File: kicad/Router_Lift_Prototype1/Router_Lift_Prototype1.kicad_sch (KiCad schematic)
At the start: 31 parts, among them J1 Conn_01x02, J10 Conn_01x02, J11 Conn_01x04, J2 Conn_01x02, J3 Conn_01x06, J4 Conn_01x06, J5 Conn_01x06, J6 Conn_01x02, J7 Conn_01x02, J8 Conn_01x02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

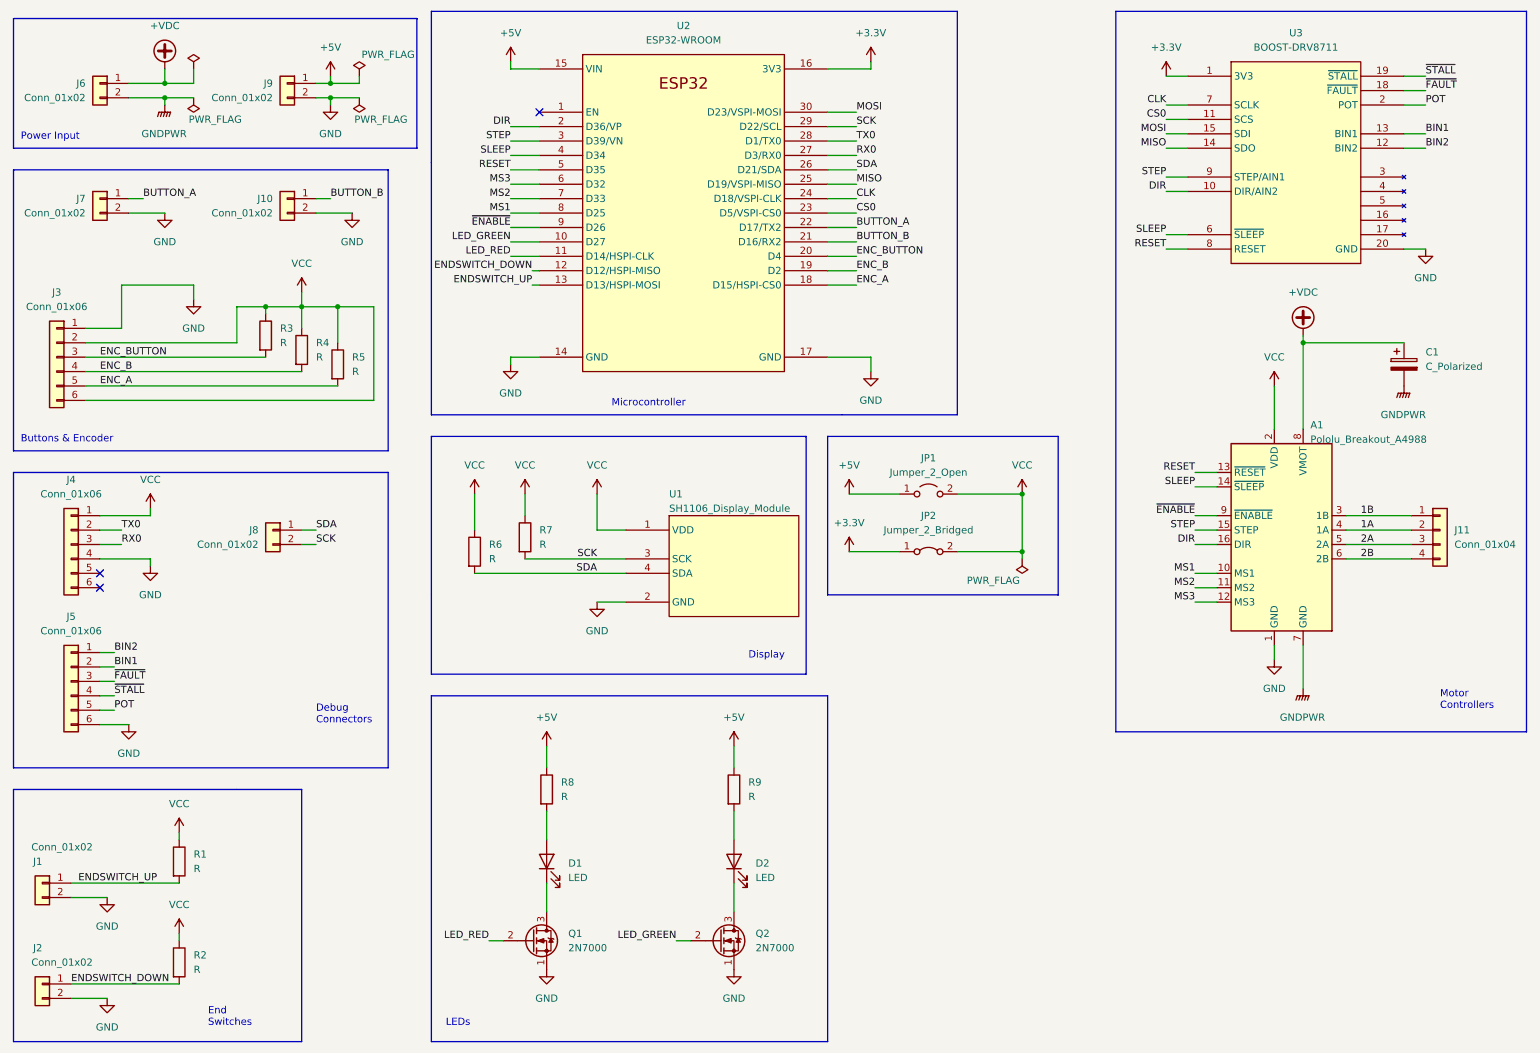
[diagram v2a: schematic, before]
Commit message: Finished routing before curving tracks and review
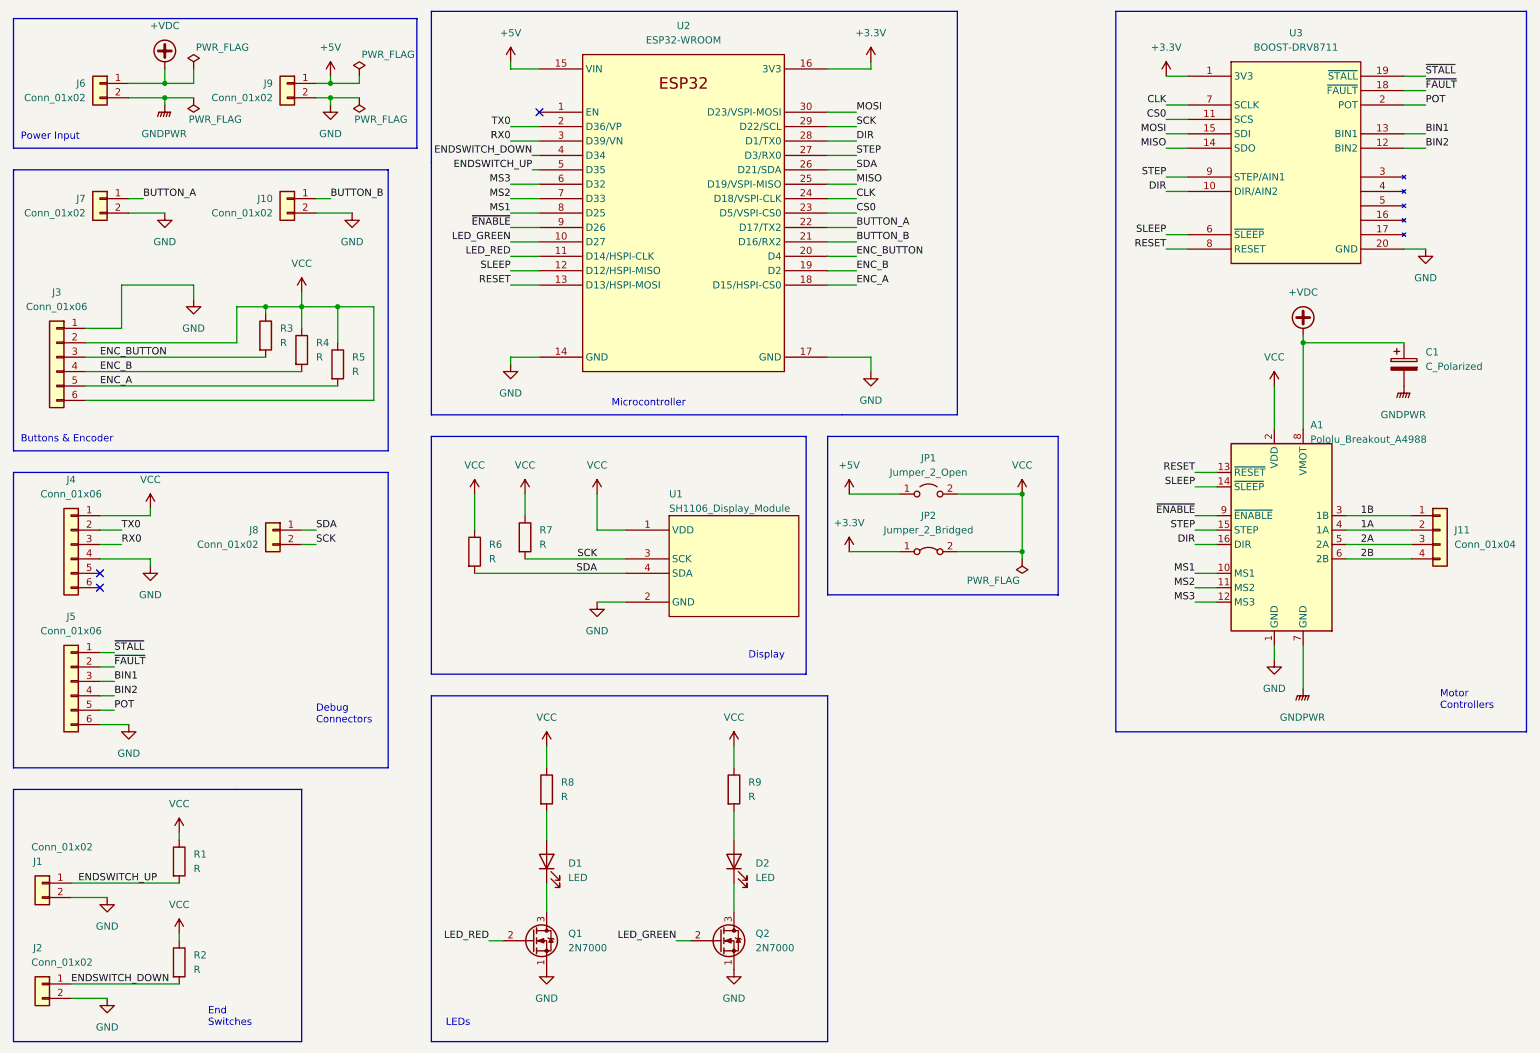
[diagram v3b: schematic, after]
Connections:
- net +5V: no longer R8.1, R9.1
- net BIN1: now also J5.3 (Pin_3); no longer J5.2 (Pin_2)
- net BIN2: now also J5.4 (Pin_4); no longer J5.1 (Pin_1)
- net DIR: now also U2.28 (D1/TX0); no longer U2.2 (D36/VP)
- net ENDSWITCH_DOWN: now also U2.4 (D34); no longer U2.12 (D12/HSPI-MISO)
- net ENDSWITCH_UP: now also U2.5 (D35); no longer U2.13 (D13/HSPI-MOSI)
- net RESET: now also U2.13 (D13/HSPI-MOSI); no longer U2.5 (D35)
- net RX0: now also U2.3 (D39/VN); no longer U2.27 (D3/RX0)
- net SLEEP: now also U2.12 (D12/HSPI-MISO); no longer U2.4 (D34)
- net STEP: now also U2.27 (D3/RX0); no longer U2.3 (D39/VN)
- net TX0: now also U2.2 (D36/VP); no longer U2.28 (D1/TX0)
- net VCC: now also R8.1, R9.1
- net ~{FAULT}: now also J5.2 (Pin_2); no longer J5.3 (Pin_3)
- net ~{STALL}: now also J5.1 (Pin_1); no longer J5.4 (Pin_4)
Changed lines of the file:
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@@
     (stroke (width 0) (type default) (color 0 0 0 0))
   )
-  (wire (pts (xy 107.95 62.23) (xy 109.22 62.23))
+  (wire (pts (xy 104.14 62.23) (xy 109.22 62.23))
     (stroke (width 0) (type default) (color 0 0 0 0))
   )
@@
     (stroke (width 0) (type default) (color 0 0 0 0))
   )
-  (wire (pts (xy 107.95 59.69) (xy 109.22 59.69))
+  (wire (pts (xy 104.14 59.69) (xy 109.22 59.69))
     (stroke (width 0) (type default) (color 0 0 0 0))
   )
@@
     (stroke (width 0) (type default) (color 0 0 0 0))
   )
-  (wire (pts (xy 104.14 41.91) (xy 109.22 41.91))
+  (wire (pts (xy 107.95 41.91) (xy 109.22 41.91))
     (stroke (width 0) (type default) (color 0 0 0 0))
   )
@@
     (stroke (width 0) (type default) (color 0 0 0 0))
   )
-  (wire (pts (xy 104.14 39.37) (xy 109.22 39.37))
+  (wire (pts (xy 107.95 39.37) (xy 109.22 39.37))
     (stroke (width 0) (type default) (color 0 0 0 0))
   )
@@
     (effects (font (size 1.27 1.27)) (justify left bottom))
   )
-  (label "ENDSWITCH_DOWN" (at 107.95 59.69 180)
+  (label "SLEEP" (at 104.14 59.69 180)
     (effects (font (size 1.27 1.27)) (justify right bottom))
   )
@@
     (effects (font (size 1.27 1.27)) (justify right bottom))
   )
-  (label "~{FAULT}" (at 34.29 132.08 0)
+  (label "BIN1" (at 34.29 132.08 0)
     (effects (font (size 1.27 1.27)) (justify left bottom))
   )
@@
     (effects (font (size 1.27 1.27)) (justify right bottom))
   )
-  (label "BIN1" (at 34.29 129.54 0)
+  (label "~{FAULT}" (at 34.29 129.54 0)
     (effects (font (size 1.27 1.27)) (justify left bottom))
   )
@@
     (effects (font (size 1.27 1.27)) (justify right bottom))
   )
-  (label "DIR" (at 104.14 34.29 180)
+  (label "TX0" (at 104.14 34.29 180)
     (effects (font (size 1.27 1.27)) (justify right bottom))
   )
@@
     (effects (font (size 1.27 1.27)) (justify left bottom))
   )
-  (label "RESET" (at 104.14 41.91 180)
-    (effects (font (size 1.27 1.27)) (justify right bottom))
-  )
-  (label "RX0" (at 165.1 39.37 0)
+  (label "ENDSWITCH_UP" (at 107.95 41.91 180)
+    (effects (font (size 1.27 1.27)) (justify right bottom))
+  )
+  (label "STEP" (at 165.1 39.37 0)
     (effects (font (size 1.27 1.27)) (justify left bottom))
   )
@@
     (effects (font (size 1.27 1.27)) (justify left bottom))
   )
-  (label "~{STALL}" (at 34.29 134.62 0)
+  (label "BIN2" (at 34.29 134.62 0)
     (effects (font (size 1.27 1.27)) (justify left bottom))
   )
@@
     (effects (font (size 1.27 1.27)) (justify left bottom))
   )
-  (label "STEP" (at 104.14 36.83 180)
+  (label "RX0" (at 104.14 36.83 180)
     (effects (font (size 1.27 1.27)) (justify right bottom))
   )
@@
     (effects (font (size 1.27 1.27)) (justify left bottom))
   )
-  (label "ENDSWITCH_UP" (at 107.95 62.23 180)
+  (label "RESET" (at 104.14 62.23 180)
     (effects (font (size 1.27 1.27)) (justify right bottom))
   )
@@
     (effects (font (size 1.27 1.27)) (justify left bottom))
   )
-  (label "SLEEP" (at 104.14 39.37 180)
+  (label "ENDSWITCH_DOWN" (at 107.95 39.37 180)
     (effects (font (size 1.27 1.27)) (justify right bottom))
   )
@@
     (effects (font (size 1.27 1.27)) (justify right bottom))
   )
-  (label "BIN2" (at 34.29 127 0)
+  (label "~{STALL}" (at 34.29 127 0)
     (effects (font (size 1.27 1.27)) (justify left bottom))
   )
@@
     (effects (font (size 1.27 1.27)) (justify left bottom))
   )
-  (label "TX0" (at 165.1 36.83 0)
+  (label "DIR" (at 165.1 36.83 0)
     (effects (font (size 1.27 1.27)) (justify left bottom))
   )
@@
   (label "CLK" (at 219.71 30.48 180)
     (effects (font (size 1.27 1.27)) (justify right bottom))
-  )
-  (symbol (lib_id "power:+5V") (at 110.49 143.51 0) (unit 1)
-    (in_bom yes) (on_board yes) (fields_autoplaced)
-    (property "Reference" "#PWR020" (id 0) (at 110.49 147.32 0)
-      (effects (font (size 1.27 1.27)) hide)
-    )
-    (property "Value" "+5V" (id 1) (at 110.49 138.43 0))
-    (property "Footprint" "" (id 2) (at 110.49 143.51 0)
-      (effects (font (size 1.27 1.27)) hide)
-    )
-    (property "Datasheet" "" (id 3) (at 110.49 143.51 0)
-      (effects (font (size 1.27 1.27)) hide)
-    )
-    (pin "1")
   )
   (symbol (lib_id "Connector_Generic:Conn_01x06") (at 24.13 74.93 0) (mirror y) (unit 1)
@@
       (effects (font (size 1.27 1.27)) hide)
     )
-    (property "Value" "" (id 1) (at 53.34 20.32 0))
+    (property "Value" "PWR_FLAG" (id 1) (at 53.34 20.32 0))
     (property "Footprint" "" (id 2) (at 48.26 24.13 0)
       (effects (font (size 1.27 1.27)) hide)
@@
     (pin "1")
   )
-  (symbol (lib_id "power:+5V") (at 143.51 143.51 0) (unit 1)
-    (in_bom yes) (on_board yes) (fields_autoplaced)
-    (property "Reference" "#PWR024" (id 0) (at 143.51 147.32 0)
-      (effects (font (size 1.27 1.27)) hide)
-    )
-    (property "Value" "+5V" (id 1) (at 143.51 138.43 0))
-    (property "Footprint" "" (id 2) (at 143.51 143.51 0)
-      (effects (font (size 1.27 1.27)) hide)
-    )
-    (property "Datasheet" "" (id 3) (at 143.51 143.51 0)
-      (effects (font (size 1.27 1.27)) hide)
-    )
-    (pin "1")
-  )
   (symbol (lib_id "Driver_Motor:BOOST-DRV8711") (at 238.76 22.86 0) (unit 1)
     (in_bom yes) (on_board yes) (fields_autoplaced)
@@
     (pin "2")
   )
+  (symbol (lib_id "power:VCC") (at 143.51 143.51 0) (unit 1)
+    (in_bom yes) (on_board yes) (fields_autoplaced)
+    (property "Reference" "#PWR0101" (id 0) (at 143.51 147.32 0)
+      (effects (font (size 1.27 1.27)) hide)
+    )
+    (property "Value" "VCC" (id 1) (at 143.51 138.43 0))
+    (property "Footprint" "" (id 2) (at 143.51 143.51 0)
+      (effects (font (size 1.27 1.27)) hide)
+    )
+    (property "Datasheet" "" (id 3) (at 143.51 143.51 0)
+      (effects (font (size 1.27 1.27)) hide)
+    )
+    (pin "1")
+  )
   (symbol (lib_id "Connector_Generic:Conn_01x02") (at 21.59 185.42 0) (mirror y) (unit 1)
     (in_bom yes) (on_board yes)
@@
     (pin "1")
   )
+  (symbol (lib_id "power:VCC") (at 110.49 143.51 0) (unit 1)
+    (in_bom yes) (on_board yes) (fields_autoplaced)
+    (property "Reference" "#PWR0102" (id 0) (at 110.49 147.32 0)
+      (effects (font (size 1.27 1.27)) hide)
+    )
+    (property "Value" "VCC" (id 1) (at 110.49 138.43 0))
+    (property "Footprint" "" (id 2) (at 110.49 143.51 0)
+      (effects (font (size 1.27 1.27)) hide)
+    )
+    (property "Datasheet" "" (id 3) (at 110.49 143.51 0)
+      (effects (font (size 1.27 1.27)) hide)
+    )
+    (pin "1")
+  )
   (symbol (lib_id "power:GND") (at 143.51 182.88 0) (unit 1)
     (in_bom yes) (on_board yes) (fields_autoplaced)
@@
       (reference "#PWR019") (unit 1) (value "VCC") (footprint "")
     )
-    (path "/00a71c34-68cb-4c27-a70b-1a03b929fc16"
-      (reference "#PWR020") (unit 1) (value "+5V") (footprint "")
-    )
     (path "/6bb4d235-2725-4be1-ab0a-0431df37ccdd"
       (reference "#PWR021") (unit 1) (value "GND") (footprint "")
@@
       (reference "#PWR023") (unit 1) (value "GND") (footprint "")
     )
-    (path "/4467ef4a-ba48-4fbd-bcde-515863e72e5a"
-      (reference "#PWR024") (unit 1) (value "+5V") (footprint "")
-    )
     (path "/e5e1e167-deb5-49f8-86ac-624780fb22d3"
       (reference "#PWR025") (unit 1) (value "GND") (footprint "")
@@
       (reference "#PWR037") (unit 1) (value "GND") (footprint "")
     )
+    (path "/908f8058-f18e-4794-8f26-b9e7a0a95f81"
+      (reference "#PWR0101") (unit 1) (value "VCC") (footprint "")
+    )
+    (path "/e42a6a7a-8964-45f9-9ec9-6998e392508a"
+      (reference "#PWR0102") (unit 1) (value "VCC") (footprint "")
+    )
     (path "/b9b39cc1-4792-4af5-ad6c-76001dfd95bd"

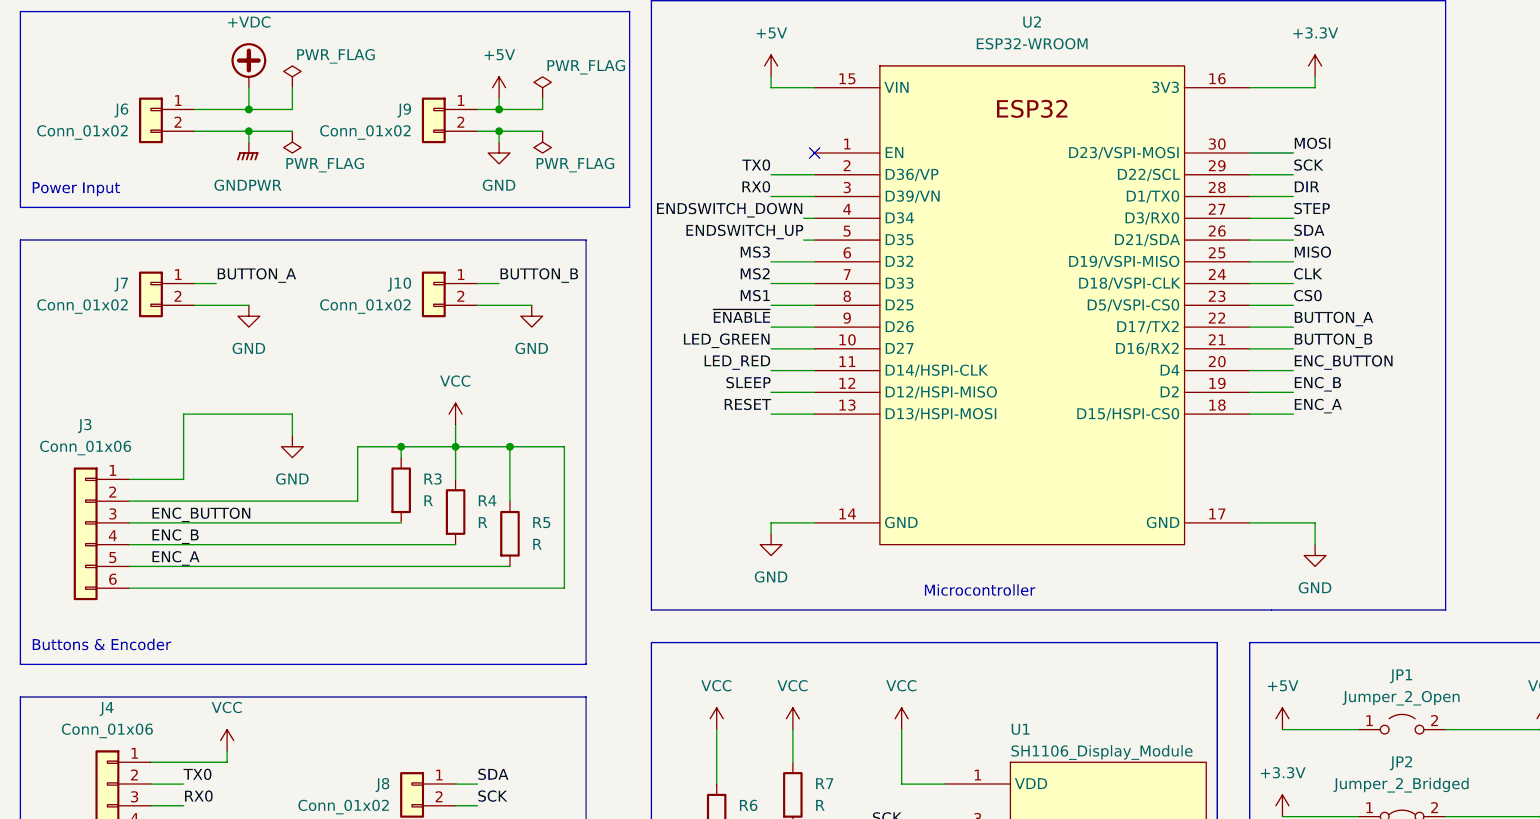
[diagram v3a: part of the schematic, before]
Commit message: Updated changes in the PCB to include SPI changes
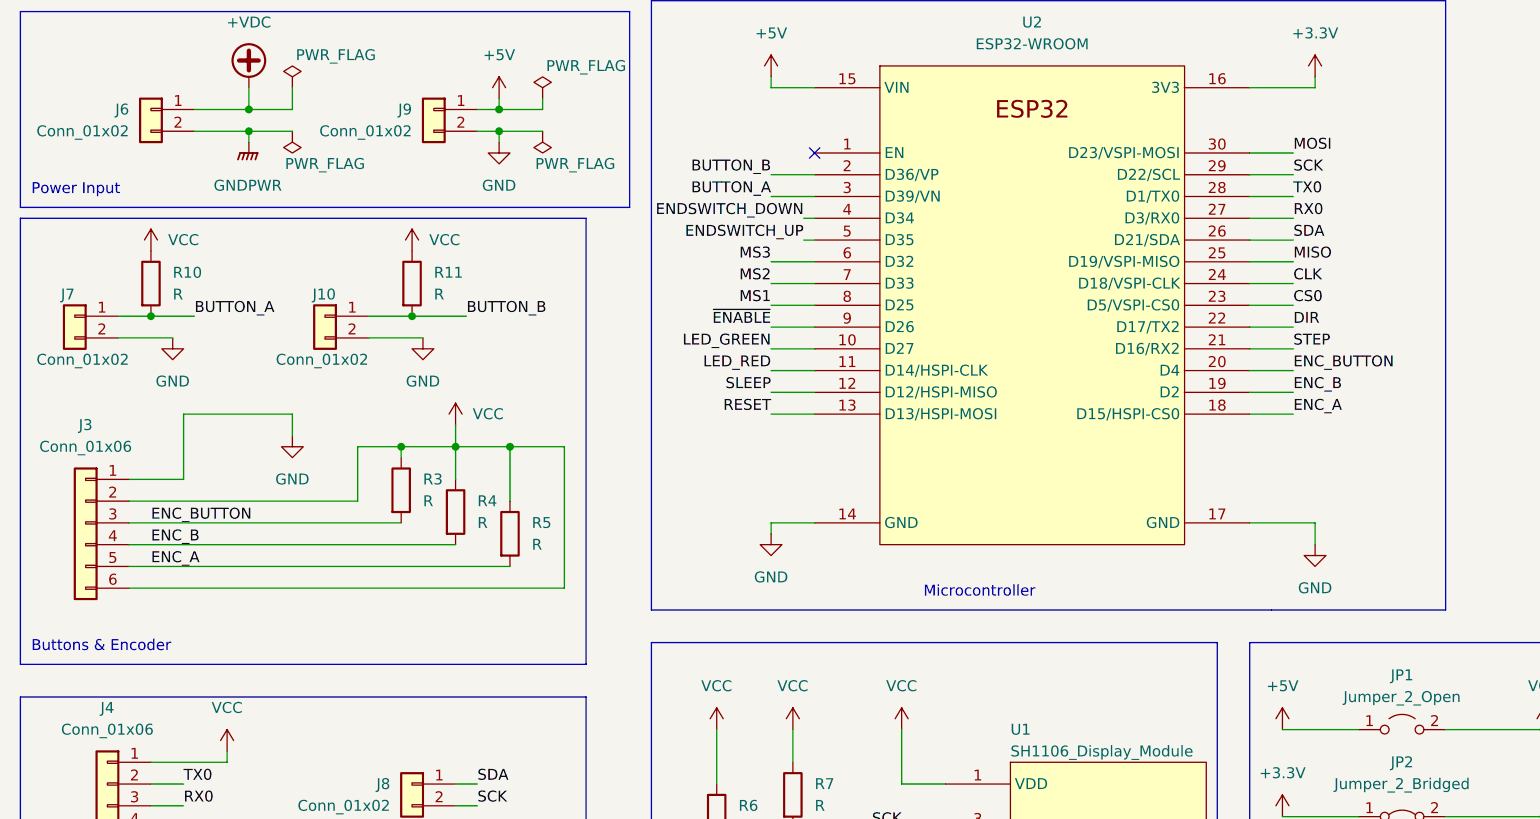
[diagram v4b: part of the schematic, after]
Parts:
- added R10, R11: R, Resistor_THT:R_Axial_DIN0207_L6.3mm_D2.5mm_P10.16mm_Horizontal, symbol Device:R
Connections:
- net BUTTON_A: now also U2.3 (D39/VN), R10.2; no longer U2.22 (D17/TX2)
- net BUTTON_B: now also U2.2 (D36/VP), R11.2; no longer U2.21 (D16/RX2)
- net DIR: now also U2.22 (D17/TX2); no longer U2.28 (D1/TX0)
- net RX0: now also U2.27 (D3/RX0); no longer U2.3 (D39/VN)
- net STEP: now also U2.21 (D16/RX2); no longer U2.27 (D3/RX0)
- net TX0: now also U2.28 (D1/TX0); no longer U2.2 (D36/VP)
- net VCC: now also R10.1, R11.1
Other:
- moved on the sheet: J10, J7
